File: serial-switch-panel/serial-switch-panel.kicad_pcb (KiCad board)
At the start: 2 copper layers, 41.9 x 31.8 mm, 58 parts, among them J10 Conn_01x01, J11 Conn_01x01, J12 Conn_01x01, J13 Conn_01x01, J14 Conn_01x01, J15 Conn_01x01, J16 Conn_01x01, J17 Conn_01x01, J18 Conn_01x01, J2 2501551-4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

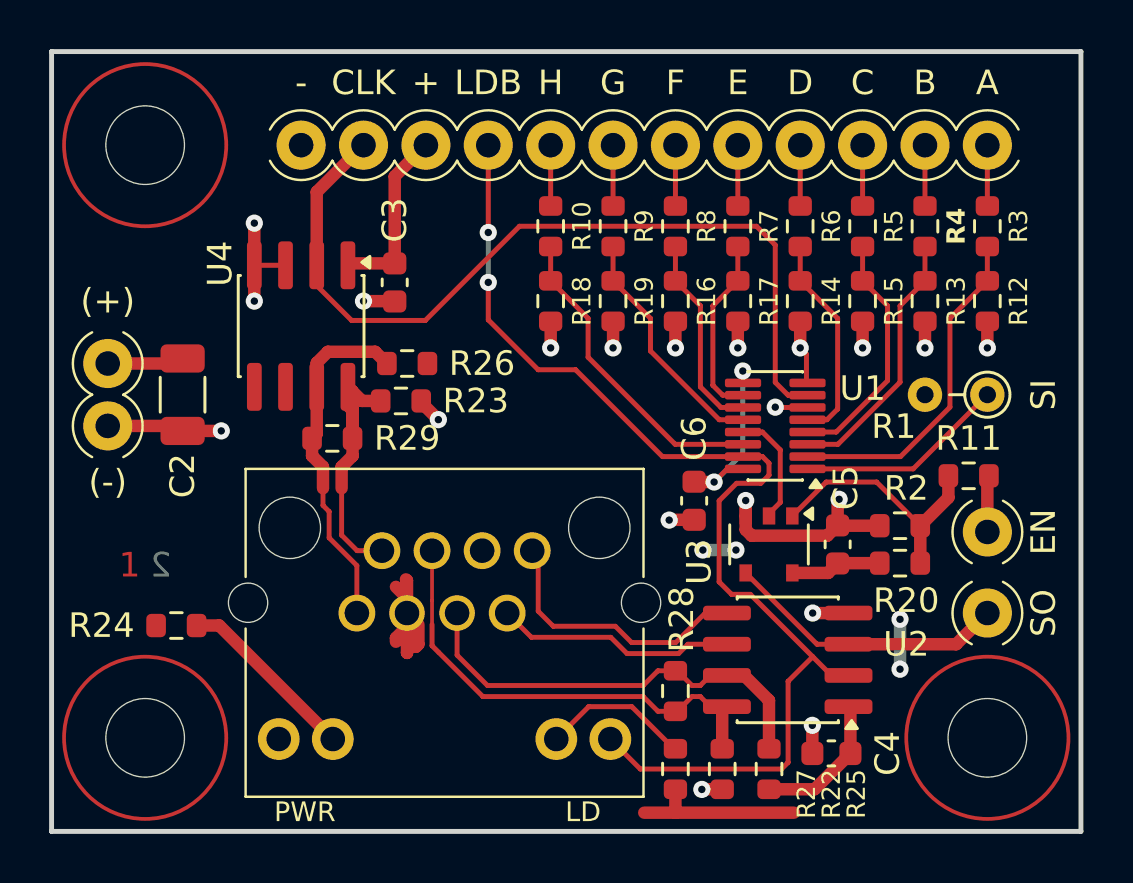
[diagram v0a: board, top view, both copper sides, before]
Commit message: [fp] Add RJ-45 shield connection
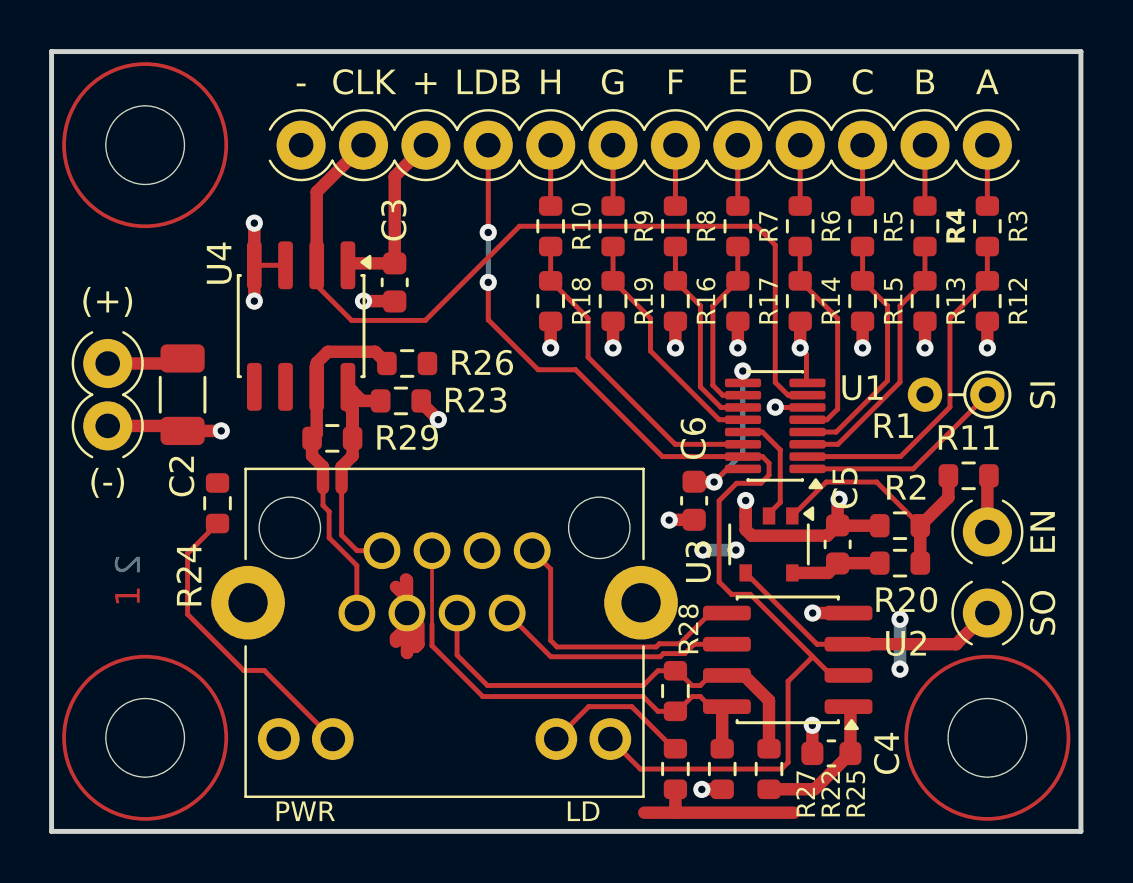
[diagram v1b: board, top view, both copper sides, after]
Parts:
- moved R24 5.25 mm to (106.8, 101.6), turned to 90 degrees
- moved LAY1 1.22 mm to (104.4, 105.4), turned to 90 degrees
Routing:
- net Net-(J2-LED1+): track 7.46 -> 12.2 mm
- net /SO_P: track 11.3 -> 11.8 mm
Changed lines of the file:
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@@
 		(tags "resistor")
 		(property "Reference" "R28"
-			(at -2.921 -0.254 90)
+			(at -2.5146 -0.5588 90)
 			(layer "F.SilkS")
 			(effects
 				(font
-					(size 1 1)
+					(size 0.8 0.8)
 					(thickness 0.15)
 				)
@@
 	(footprint "Resistor_SMD:R_0603_1608Metric"
 		(layer "F.Cu")
-		(at 105.08 106.618 180)
+		(at 106.7564 101.6396 90)
 		(descr "Resistor SMD 0603 (1608 Metric), square (rectangular) end terminal, IPC-7351 nominal, (Body size source: IPC-SM-782 page 72, https://www.pcb-3d.com/wordpress/wp-content/uploads/ipc-sm-782a_amendment_1_and_2.pdf), generated with kicad-footprint-generator")
 		(tags "resistor")
 		(property "Reference" "R24"
-			(at 3.048 0 0)
+			(at -2.9464 -1.1176 90)
 			(layer "F.SilkS")
 			(effects
@@
 		)
 		(property "Value" "1k"
-			(at 0 1.43 0)
+			(at 0 1.43 90)
 			(layer "F.Fab")
 			(hide yes)
@@
 		)
 		(property "Datasheet" ""
-			(at 0 0 0)
+			(at 0 0 90)
 			(layer "F.Fab")
 			(hide yes)
@@
 		)
 		(property "Description" "Resistor"
-			(at 0 0 0)
+			(at 0 0 90)
 			(layer "F.Fab")
 			(hide yes)
@@
 		(duplicate_pad_numbers_are_jumpers no)
 		(fp_line
-			(start -0.237258 0.5225)
-			(end 0.237258 0.5225)
+			(start -0.237258 -0.5225)
+			(end 0.237258 -0.5225)
 			(stroke
 				(width 0.12)
@@
 		)
 		(fp_line
-			(start -0.237258 -0.5225)
-			(end 0.237258 -0.5225)
+			(start -0.237258 0.5225)
+			(end 0.237258 0.5225)
 			(stroke
 				(width 0.12)
@@
 		)
 		(fp_text user "${REFERENCE}"
-			(at 0 0 0)
+			(at 0 0 90)
 			(layer "F.Fab")
 			(effects
@@
 		)
 		(pad "1" smd roundrect
-			(at -0.825 0 180)
+			(at -0.825 0 90)
 			(size 0.8 0.95)
 			(layers "F.Cu" "F.Mask" "F.Paste")
@@
 		)
 		(pad "2" smd roundrect
-			(at 0.825 0 180)
+			(at 0.825 0 90)
 			(size 0.8 0.95)
 			(layers "F.Cu" "F.Mask" "F.Paste")
@@
 	(footprint "Symbol:LayerMarker_2_3.81x2.54mm_TextH1mm_P1.27mm_BottomMirrored"
 		(layer "F.Cu")
-		(at 103.175 105.4262)
+		(at 104.3962 105.4242 90)
 		(descr "Layer marker, 2 layers, simple ordinals, text size 1mm, pitch 1.27mm, margin 1.27mm")
 		(tags "layer order identification numbering")
 		(property "Reference" "LAY1"
-			(at 0 1.27 0)
+			(at 0 1.27 90)
 			(layer "F.SilkS")
 			(hide yes)
@@
 		)
 		(property "Value" "~"
-			(at 0 2.54 0)
+			(at 0 2.54 90)
 			(layer "F.Fab")
 			(hide yes)
@@
 		)
 		(property "Datasheet" ""
-			(at 0 0 0)
+			(at 0 0 90)
 			(layer "F.Fab")
 			(hide yes)
@@
 		)
 		(property "Description" ""
-			(at 0 0 0)
+			(at 0 0 90)
 			(layer "F.Fab")
 			(hide yes)
@@
 		(duplicate_pad_numbers_are_jumpers no)
 		(fp_text user "1"
-			(at 0 -1.27 0)
+			(at 0 -1.27 90)
 			(layer "F.Cu")
 			(effects
@@
 		)
 		(fp_text user "2"
-			(at 1.27 -1.27 0)
+			(at 1.27 -1.27 90)
 			(layer "B.Cu")
 			(effects
@@
 			(polygon
 				(pts
-					(xy 101.905 102.8862) (xy 105.715 102.8862) (xy 105.715 105.4262) (xy 101.905 105.4262)
+					(xy 101.8562 106.6942) (xy 101.8562 102.8842) (xy 104.3962 102.8842) (xy 104.3962 106.6942)
 				)
 			)
@@
 			(unit
 				(name "A")
-				(pins "1" "2" "3" "6" "5" "4" "7" "8" "10" "9" "12" "11")
+				(pins "1" "2" "3" "6" "5" "4" "7" "8" "10" "9" "12" "11" "S")
 			)
 		)
@@
 		)
 		(fp_line
-			(start -1.8 2)
+			(start -1.8 1.27)
 			(end -1.8 -2.4)
 			(stroke
@@
 		(fp_line
 			(start -1.8 10.95)
-			(end -1.8 4.1)
+			(end -1.8 4.826)
 			(stroke
 				(width 0.1)
@@
 		)
 		(fp_line
-			(start 14.4 2)
+			(start 14.4 1.27)
 			(end 14.4 -2.4)
 			(stroke
@@
 		(fp_line
 			(start 14.4 10.95)
-			(end 14.4 4.1)
+			(end 14.4 4.826)
 			(stroke
 				(width 0.1)
@@
 		)
 		(pad "" np_thru_hole circle
-			(at -1.7 3.05)
-			(size 1.6 1.6)
-			(drill 1.6)
-			(layers "*.Mask")
-		)
-		(pad "" np_thru_hole circle
 			(at 0 0)
 			(size 2.5 2.5)
@@
 			(layers "*.Mask")
 		)
-		(pad "" np_thru_hole circle
-			(at 14.3 3.05)
-			(size 1.6 1.6)
-			(drill 1.6)
-			(layers "*.Mask")
-		)
 		(pad "1" thru_hole circle
 			(at 2.73 3.47)
@@
 		(pad "3" thru_hole circle
 			(at 4.77 3.47)
-			(size 1.45 1.45)
+			(size 1.5 1.5)
 			(drill 1)
 			(layers "*.Cu" "*.Mask")
@@
 		(pad "5" thru_hole circle
 			(at 6.81 3.47)
-			(size 1.45 1.45)
+			(size 1.5 1.5)
 			(drill 1)
 			(layers "*.Cu" "*.Mask")
@@
 			(pintype "passive")
 		)
+		(pad "S" thru_hole circle
+			(at -1.7 3.05)
+			(size 3 3)
+			(drill 1.6)
+			(layers "*.Cu" "*.Mask")
+			(remove_unused_layers no)
+			(net "GND")
+			(pinfunction "SHIELD_S")
+			(pintype "input")
+		)
+		(pad "S" thru_hole circle
+			(at 14.3 3.05)
+			(size 3 3)
+			(drill 1.6)
+			(layers "*.Cu" "*.Mask")
+			(remove_unused_layers no)
+			(net "GND")
+			(pinfunction "SHIELD_S")
+			(pintype "input")
+		)
 		(embedded_fonts no)
 	)
@@
 	)
 	(segment
-		(start 123.616198 107.31)
-		(end 122.953198 106.647)
+		(start 120.32 107.2276)
+		(end 120.32 104.32)
 		(width 0.2)
 		(layer "F.Cu")
@@
 	)
 	(segment
-		(start 122.953198 106.647)
-		(end 120.425199 106.647)
+		(start 120.5824 107.49)
+		(end 120.32 107.2276)
 		(width 0.2)
 		(layer "F.Cu")
@@
 	)
 	(segment
-		(start 119.812 106.033801)
-		(end 119.812 103.812)
+		(start 124.746666 107.36)
+		(end 124.616667 107.49)
 		(width 0.2)
 		(layer "F.Cu")
@@
 	)
 	(segment
-		(start 120.425199 106.647)
-		(end 119.812 106.033801)
+		(start 125.5724 107.36)
+		(end 124.746666 107.36)
 		(width 0.2)
 		(layer "F.Cu")
@@
 	)
 	(segment
-		(start 126.612314 106.11)
-		(end 125.412314 107.31)
+		(start 127.497 106.11)
+		(end 126.8224 106.11)
 		(width 0.2)
 		(layer "F.Cu")
@@
 	)
 	(segment
-		(start 127.497 106.11)
-		(end 126.612314 106.11)
+		(start 120.32 104.32)
+		(end 119.57 103.57)
 		(width 0.2)
 		(layer "F.Cu")
@@
 	)
 	(segment
-		(start 119.812 103.812)
-		(end 119.57 103.57)
+		(start 126.8224 106.11)
+		(end 125.5724 107.36)
 		(width 0.2)
 		(layer "F.Cu")
@@
 	)
 	(segment
-		(start 125.412314 107.31)
-		(end 123.616198 107.31)
+		(start 124.616667 107.49)
+		(end 120.5824 107.49)
 		(width 0.2)
 		(layer "F.Cu")
@@
 	)
 	(segment
-		(start 125.528 107.76)
-		(end 123.429802 107.76)
+		(start 124.782352 107.89)
+		(end 120.33 107.89)
 		(width 0.2)
 		(layer "F.Cu")
@@
 	)
 	(segment
-		(start 123.429802 107.76)
-		(end 122.766802 107.097)
+		(start 126.162 107.38)
+		(end 125.782 107.76)
 		(width 0.2)
 		(layer "F.Cu")
@@
 	)
 	(segment
-		(start 122.766802 107.097)
-		(end 119.537 107.097)
+		(start 124.912353 107.76)
+		(end 124.782352 107.89)
 		(width 0.2)
 		(layer "F.Cu")
@@
 	)
 	(segment
-		(start 125.908 107.38)
-		(end 125.528 107.76)
+		(start 120.33 107.89)
+		(end 118.55 106.11)
 		(width 0.2)
 		(layer "F.Cu")
@@
 	(segment
 		(start 127.497 107.38)
-		(end 125.908 107.38)
+		(end 126.162 107.38)
 		(width 0.2)
 		(layer "F.Cu")
@@
 	)
 	(segment
-		(start 119.537 107.097)
-		(end 118.55 106.11)
+		(start 125.782 107.76)
+		(end 124.912353 107.76)
 		(width 0.2)
 		(layer "F.Cu")
@@
 	)
 	(segment
-		(start 106.828 106.618)
-		(end 111.45 111.24)
-		(width 0.508)
+		(start 107.8232 108.4468)
+		(end 105.5372 106.1608)
+		(width 0.2)
 		(layer "F.Cu")
 		(net "Net-(J2-LED1+)")
 	)
 	(segment
-		(start 105.905 106.618)
-		(end 106.828 106.618)
-		(width 0.508)
+		(start 105.5372 106.1608)
+		(end 105.5372 103.6838)
+		(width 0.2)
+		(layer "F.Cu")
+		(net "Net-(J2-LED1+)")
+	)
+	(segment
+		(start 105.5372 103.6838)
+		(end 106.7564 102.4646)
+		(width 0.2)
+		(layer "F.Cu")
+		(net "Net-(J2-LED1+)")
+	)
+	(segment
+		(start 111.45 111.24)
+		(end 108.6568 108.4468)
+		(width 0.2)
+		(layer "F.Cu")
+		(net "Net-(J2-LED1+)")
+	)
+	(segment
+		(start 108.6568 108.4468)
+		(end 107.8232 108.4468)
+		(width 0.2)
 		(layer "F.Cu")
 		(net "Net-(J2-LED1+)")

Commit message: [fp] Change '166 to SOIC-16 footprint; Export v1.0A1 gerbers
Wow, that one is tight (!)
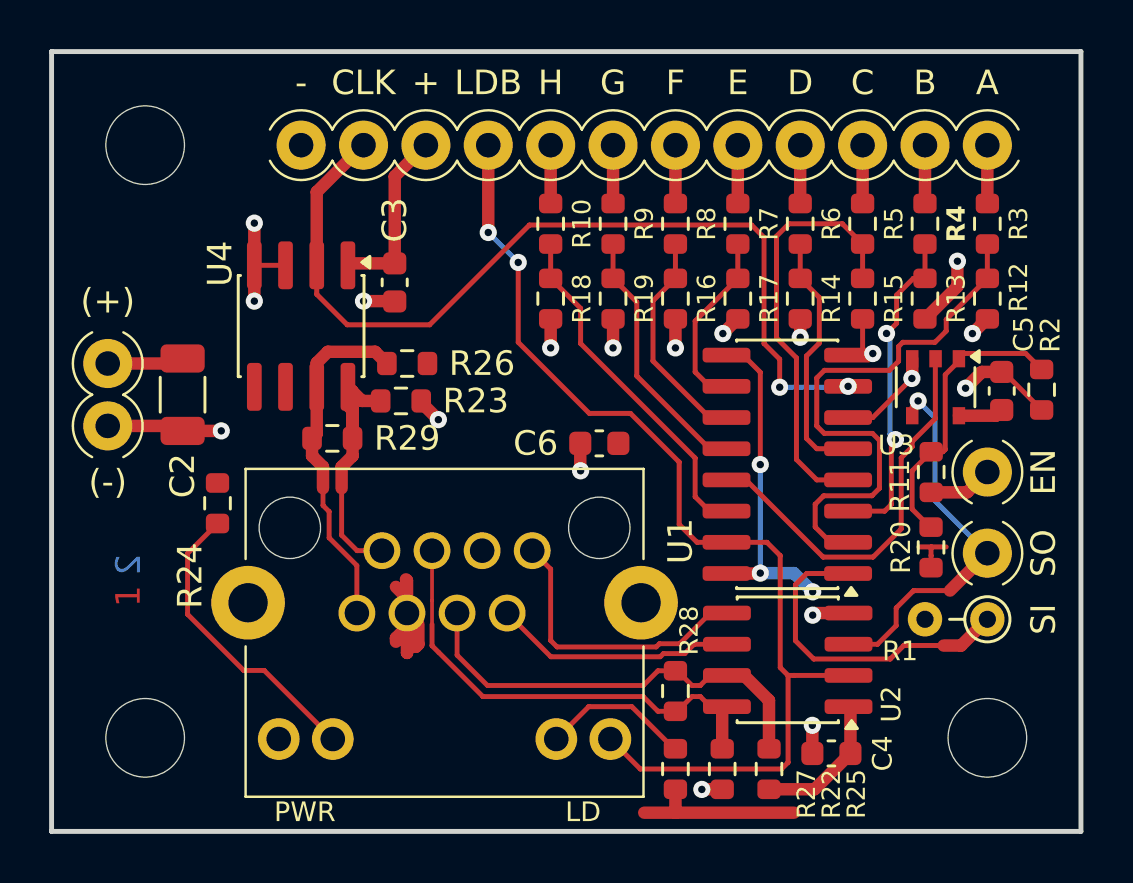
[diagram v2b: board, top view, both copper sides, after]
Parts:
- U1: value 74LS166 -> 74HCS166; footprint Package_SO:Texas_DYY0016A_TSOT-23-16_2x4.2mm_P0.5mm -> Package_SO:SOIC-16_3.9x9.9mm_P1.27mm
- moved U3 9.33 mm to (136.0, 96.9)
- moved C5 9.15 mm to (138.7, 97.1)
- moved R1 9.14 mm to (138.1, 106.4)
- moved R2 7.99 mm to (140.3, 97.0), turned to -90 degrees
- moved C6 4.51 mm to (122.3, 99.2), turned to 180 degrees
- moved J11 2.44 mm to (138.1, 100.4)
- moved J12 2.44 mm to (138.1, 103.7)
- moved U1 1.64 mm to (130.0, 100.1)
- moved R11 1.53 mm to (135.8, 100.4), turned to 90 degrees
- moved R20 1.42 mm to (135.8, 103.4), turned to 90 degrees
- moved R10 0.10 mm to (120.3, 90.3)
- moved R12 0.10 mm to (138.1, 93.3)
- moved R13 0.10 mm to (135.6, 93.3)
- moved R14 0.10 mm to (130.5, 93.3)
- moved R15 0.10 mm to (133.0, 93.3)
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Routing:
- net Net-(U1-Qh): track 4.70 -> 16.5 mm
- net /IN_A: track 13.8 -> 22.8 mm
- net /IN_C: track 10.0 -> 17.3 mm
- net /SCAN_IN: track 8.57 -> 13.4 mm
- net /SCAN_OUT: track 11.6 -> 15.7 mm, vias 0 -> 1
- net /LOADB: track 46.6 -> 43.1 mm
- net /IN_B: track 10.8 -> 13.6 mm, vias 0 -> 2
- net +5V: track 47.0 -> 48.9 mm, vias 6 -> 3
- net /CLK: track 34.8 -> 36.6 mm, vias 0 -> 2
- net /IN_D: track 8.66 -> 10.3 mm
- net Net-(R11-Pad2): track 10.5 -> 12.0 mm
- net /IN_H: track 13.1 -> 14.2 mm
- net /IN_F: track 8.22 -> 9.09 mm
- net /IN_G: track 9.81 -> 10.7 mm
- net GND: track 35.5 -> 35.9 mm, vias 20 -> 19
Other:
- board text added: "Power Control Input Board (C) Electronics Tinkerer 2026-03-09 v1.0A"
- board text removed: "Power Control Input Board (C) Electronics Tinkerer 2026-03-07 v1.0A"

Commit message: [fp] Update DRC rules; bump PCB to v1.0B
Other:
- board text added: "Power Control Input Board (C) Electronics Tinkerer 2026-05-29 v1.0B"
- board text removed: "Power Control Input Board (C) Electronics Tinkerer 2026-03-09 v1.0A"
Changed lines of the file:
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@@
 		(0 "F.Cu" signal)
 		(2 "B.Cu" signal)
-		(9 "F.Adhes" user "F.Adhesive")
-		(11 "B.Adhes" user "B.Adhesive")
 		(13 "F.Paste" user)
 		(15 "B.Paste" user)
@@
 		(17 "Dwgs.User" user "User.Drawings")
 		(19 "Cmts.User" user "User.Comments")
-		(21 "Eco1.User" user "User.Eco1")
-		(23 "Eco2.User" user "User.Eco2")
 		(25 "Edge.Cuts" user)
 		(27 "Margin" user)
@@
 		(35 "F.Fab" user)
 		(33 "B.Fab" user)
-		(39 "User.1" user)
-		(41 "User.2" user)
-		(43 "User.3" user)
-		(45 "User.4" user)
 	)
 	(setup
@@
 				(type "Bottom Silk Screen")
 			)
-			(copper_finish "HAL lead-free")
+			(copper_finish "None")
 			(dielectric_constraints no)
 		)
 		(pad_to_mask_clearance 0)
-		(allow_soldermask_bridges_in_footprints yes)
+		(allow_soldermask_bridges_in_footprints no)
 		(tenting
 			(front yes)
@@
 		)
 	)
-	(gr_text "Power Control Input Board\n(C) Electronics Tinkerer\n2026-03-09 v1.0A"
+	(gr_text "Power Control Input Board\n(C) Electronics Tinkerer\n2026-05-29 v1.0B"
 		(at 129.208 91.7844 0)
 		(layer "B.SilkS")
@@
 			(keep_text_aligned yes)
 		)
-		(gr_text "24.13"
+		(gr_text "0.95"
 			(at 93.262 99.125 90)
 			(layer "Dwgs.User")
@@
 			(keep_text_aligned yes)
 		)
-		(gr_text "34.29"
+		(gr_text "1.35"
 			(at 120.955 121.012 0)
 			(layer "Dwgs.User")
@@
 			(keep_text_aligned yes)
 		)
-		(gr_text "31.75"
+		(gr_text "1.25"
 			(at 146.602 99.125 90)
 			(layer "Dwgs.User")
@@
 			(keep_text_aligned yes)
 		)
-		(gr_text "41.91"
+		(gr_text "1.65"
 			(at 120.955 78.29 0)
 			(layer "Dwgs.User")
